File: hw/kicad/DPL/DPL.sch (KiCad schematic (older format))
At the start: 30 parts, among them J0 Programer, J1 DPL1, J2 DPL2, J3 DPL3, J4 DPL4, J5 DPL5, J6 DPL6, Q1 IRF540N, Q2 IRF540N, Q3 IRF540N, Q4 IRF540N, Q5 IRF540N, Q6 IRF540N, SW1 SW_Reed, SW2 SW_Reed, SW3 SW_Reed, SW4 SW_Reed, SW5 SW_Reed, SW6 SW_Reed, U0 SAMD21E, U1 Payload, Y1 32.768kHz

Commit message: Added power selector to the board. Started to design the footprint's layout.
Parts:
- added JP1: Power selector, Connector_PinHeader_2.54mm:PinHeader_1x03_P2.54mm_Vertical, symbol Device:Jumper_NC_Dual
- added R0: 1k, Resistor_THT:R_Axial_DIN0207_L6.3mm_D2.5mm_P10.16mm_Horizontal, symbol Device:R
- C1a1, C1b1: footprint (none) -> Capacitor_SMD:C_0603_1608Metric_Pad1.05x0.95mm_HandSolder
- J0: footprint (none) -> Connector_PinHeader_2.54mm:PinHeader_1x05_P2.54mm_Vertical
- J1, J2, J3, J4, J5, J6: footprint (none) -> TerminalBlock:TerminalBlock_Altech_AK300-2_P5.00mm
- R1, R2, R3, R4, R5, R6: footprint (none) -> Resistor_THT:R_Axial_DIN0207_L6.3mm_D2.5mm_P10.16mm_Horizontal
- SW1, SW2, SW3, SW4, SW5, SW6: footprint (none) -> Resistor_THT:R_Axial_DIN0309_L9.0mm_D3.2mm_P15.24mm_Horizontal
- U0: footprint (none) -> Package_QFP:TQFP-32_7x7mm_P0.8mm
- U1: footprint (none) -> Payload:PC104-Standard
- Y1: footprint (none) -> Crystal:Crystal_SMD_EuroQuartz_EQ161-2Pin_3.2x1.5mm_HandSoldering
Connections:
- net 3V3: now also R0.1
- net 5V0: now also JP1.3
- net SWCLK: now also R0.2
- net VBUS: now also JP1.1
- net VIN: now also JP1.2
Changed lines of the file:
@@
 F 0 "U1" H 9000 4798 50  0000 C CNN
 F 1 "Payload" H 9000 4707 50  0000 C CNN
-F 2 "" H 7900 4050 50  0001 C CNN
+F 2 "Payload:PC104-Standard" H 7900 4050 50  0001 C CNN
 F 3 "" H 7900 4050 50  0001 C CNN
 	1    9000 3250
@@
 F 0 "J1" H 1480 4442 50  0000 L CNN
 F 1 "DPL1" H 1480 4351 50  0000 L CNN
-F 2 "" H 1400 4450 50  0001 C CNN
+F 2 "TerminalBlock:TerminalBlock_Altech_AK300-2_P5.00mm" H 1400 4450 50  0001 C CNN
 F 3 "~" H 1400 4450 50  0001 C CNN
 	1    1400 4450
@@
 F 0 "J2" H 2630 4442 50  0000 L CNN
 F 1 "DPL2" H 2630 4351 50  0000 L CNN
-F 2 "" H 2550 4450 50  0001 C CNN
+F 2 "TerminalBlock:TerminalBlock_Altech_AK300-2_P5.00mm" H 2550 4450 50  0001 C CNN
 F 3 "~" H 2550 4450 50  0001 C CNN
 	1    2550 4450
@@
 F 0 "J3" H 3780 4442 50  0000 L CNN
 F 1 "DPL3" H 3780 4351 50  0000 L CNN
-F 2 "" H 3700 4450 50  0001 C CNN
+F 2 "TerminalBlock:TerminalBlock_Altech_AK300-2_P5.00mm" H 3700 4450 50  0001 C CNN
 F 3 "~" H 3700 4450 50  0001 C CNN
 	1    3700 4450
@@
 F 0 "J4" H 1480 5342 50  0000 L CNN
 F 1 "DPL4" H 1480 5251 50  0000 L CNN
-F 2 "" H 1400 5350 50  0001 C CNN
+F 2 "TerminalBlock:TerminalBlock_Altech_AK300-2_P5.00mm" H 1400 5350 50  0001 C CNN
 F 3 "~" H 1400 5350 50  0001 C CNN
 	1    1400 5350
@@
 F 0 "J5" H 2630 5342 50  0000 L CNN
 F 1 "DPL5" H 2630 5251 50  0000 L CNN
-F 2 "" H 2550 5350 50  0001 C CNN
+F 2 "TerminalBlock:TerminalBlock_Altech_AK300-2_P5.00mm" H 2550 5350 50  0001 C CNN
 F 3 "~" H 2550 5350 50  0001 C CNN
 	1    2550 5350
@@
 F 0 "J6" H 3780 5342 50  0000 L CNN
 F 1 "DPL6" H 3780 5251 50  0000 L CNN
-F 2 "" H 3700 5350 50  0001 C CNN
+F 2 "TerminalBlock:TerminalBlock_Altech_AK300-2_P5.00mm" H 3700 5350 50  0001 C CNN
 F 3 "~" H 3700 5350 50  0001 C CNN
 	1    3700 5350
@@
 F 0 "U0" H 5250 4215 50  0000 C CNN
 F 1 "SAMD21E" H 5250 4124 50  0000 C CNN
-F 2 "" H 5250 3100 50  0001 C CNN
+F 2 "Package_QFP:TQFP-32_7x7mm_P0.8mm" H 5250 3100 50  0001 C CNN
 F 3 "" H 5250 3100 50  0001 C CNN
 	1    5250 3200
@@
 F 0 "J0" H 4058 1681 50  0000 C CNN
 F 1 "Programer" H 4058 1590 50  0000 C CNN
-F 2 "" H 3950 1300 50  0001 C CNN
+F 2 "Connector_PinHeader_2.54mm:PinHeader_1x05_P2.54mm_Vertical" H 3950 1300 50  0001 C CNN
 F 3 "~" H 3950 1300 50  0001 C CNN
 	1    3950 1300
@@
 F 0 "Y1" H 3950 2768 50  0000 C CNN
 F 1 "32.768kHz" H 3950 2677 50  0000 C CNN
-F 2 "" H 3950 2500 50  0001 C CNN
+F 2 "Crystal:Crystal_SMD_EuroQuartz_EQ161-2Pin_3.2x1.5mm_HandSoldering" H 3950 2500 50  0001 C CNN
 F 3 "~" H 3950 2500 50  0001 C CNN
 	1    3950 2500
@@
 F 0 "C1b1" H 3715 2796 50  0000 L CNN
 F 1 "9pF" H 3715 2705 50  0000 L CNN
-F 2 "" H 3638 2600 50  0001 C CNN
+F 2 "Capacitor_SMD:C_0603_1608Metric_Pad1.05x0.95mm_HandSolder" H 3638 2600 50  0001 C CNN
 F 3 "~" H 3600 2750 50  0001 C CNN
 	1    3600 2750
@@
 F 0 "C1a1" H 3715 2296 50  0000 L CNN
 F 1 "9pF" H 3715 2205 50  0000 L CNN
-F 2 "" H 3638 2100 50  0001 C CNN
+F 2 "Capacitor_SMD:C_0603_1608Metric_Pad1.05x0.95mm_HandSolder" H 3638 2100 50  0001 C CNN
 F 3 "~" H 3600 2250 50  0001 C CNN
 	1    3600 2250
@@
 	1050 5000 1050 5050
 $Comp
-L power:GND #PWR?
+L power:GND #PWR0101
 U 1 1 5CF99838
 P 1050 5050
-F 0 "#PWR?" H 1050 4800 50  0001 C CNN
+F 0 "#PWR0101" H 1050 4800 50  0001 C CNN
 F 1 "GND" H 1055 4877 50  0000 C CNN
 F 2 "" H 1050 5050 50  0001 C CNN
@@
 	2200 5000 2200 5050
 $Comp
-L power:GND #PWR?
+L power:GND #PWR0104
 U 1 1 5CF9AF8D
 P 2200 5050
-F 0 "#PWR?" H 2200 4800 50  0001 C CNN
+F 0 "#PWR0104" H 2200 4800 50  0001 C CNN
 F 1 "GND" H 2205 4877 50  0000 C CNN
 F 2 "" H 2200 5050 50  0001 C CNN
@@
 	3350 5000 3350 5050
 $Comp
-L power:GND #PWR?
+L power:GND #PWR0105
 U 1 1 5CF9BBE1
 P 3350 5050
-F 0 "#PWR?" H 3350 4800 50  0001 C CNN
+F 0 "#PWR0105" H 3350 4800 50  0001 C CNN
 F 1 "GND" H 3355 4877 50  0000 C CNN
 F 2 "" H 3350 5050 50  0001 C CNN
@@
 	1050 5900 1050 5950
 $Comp
-L power:GND #PWR?
+L power:GND #PWR0106
 U 1 1 5CF9C528
 P 1050 5950
-F 0 "#PWR?" H 1050 5700 50  0001 C CNN
+F 0 "#PWR0106" H 1050 5700 50  0001 C CNN
 F 1 "GND" H 1055 5777 50  0000 C CNN
 F 2 "" H 1050 5950 50  0001 C CNN
@@
 	2350 5350 2200 5350
 $Comp
-L power:GND #PWR?
+L power:GND #PWR0109
 U 1 1 5CF9CBDF
 P 2200 5950
-F 0 "#PWR?" H 2200 5700 50  0001 C CNN
+F 0 "#PWR0109" H 2200 5700 50  0001 C CNN
 F 1 "GND" H 2205 5777 50  0000 C CNN
 F 2 "" H 2200 5950 50  0001 C CNN
@@
 	3350 5350 3500 5350
 $Comp
-L power:GND #PWR?
+L power:GND #PWR0110
 U 1 1 5CF9D59C
 P 3350 5950
-F 0 "#PWR?" H 3350 5700 50  0001 C CNN
+F 0 "#PWR0110" H 3350 5700 50  0001 C CNN
 F 1 "GND" H 3355 5777 50  0000 C CNN
 F 2 "" H 3350 5950 50  0001 C CNN
@@
 Connection ~ 3400 2750
 $Comp
-L power:GND #PWR?
+L power:GND #PWR0111
 U 1 1 5CF9C5E9
 P 3400 2800
-F 0 "#PWR?" H 3400 2550 50  0001 C CNN
+F 0 "#PWR0111" H 3400 2550 50  0001 C CNN
 F 1 "GND" H 3405 2627 50  0000 C CNN
 F 2 "" H 3400 2800 50  0001 C CNN
@@
 F 0 "SW1" H 4850 5672 50  0000 C CNN
 F 1 "SW_Reed" H 4850 5581 50  0000 C CNN
-F 2 "" H 4850 5450 50  0001 C CNN
+F 2 "Resistor_THT:R_Axial_DIN0309_L9.0mm_D3.2mm_P15.24mm_Horizontal" H 4850 5450 50  0001 C CNN
 F 3 "~" H 4850 5450 50  0001 C CNN
 	1    4850 5450
@@
 F 0 "SW2" H 4850 6022 50  0000 C CNN
 F 1 "SW_Reed" H 4850 5931 50  0000 C CNN
-F 2 "" H 4850 5800 50  0001 C CNN
+F 2 "Resistor_THT:R_Axial_DIN0309_L9.0mm_D3.2mm_P15.24mm_Horizontal" H 4850 5800 50  0001 C CNN
 F 3 "~" H 4850 5800 50  0001 C CNN
 	1    4850 5800
@@
 F 0 "SW3" H 4850 6372 50  0000 C CNN
 F 1 "SW_Reed" H 4850 6281 50  0000 C CNN
-F 2 "" H 4850 6150 50  0001 C CNN
+F 2 "Resistor_THT:R_Axial_DIN0309_L9.0mm_D3.2mm_P15.24mm_Horizontal" H 4850 6150 50  0001 C CNN
 F 3 "~" H 4850 6150 50  0001 C CNN
 	1    4850 6150
@@
 F 0 "SW4" H 4850 6722 50  0000 C CNN
 F 1 "SW_Reed" H 4850 6631 50  0000 C CNN
-F 2 "" H 4850 6500 50  0001 C CNN
+F 2 "Resistor_THT:R_Axial_DIN0309_L9.0mm_D3.2mm_P15.24mm_Horizontal" H 4850 6500 50  0001 C CNN
 F 3 "~" H 4850 6500 50  0001 C CNN
 	1    4850 6500
@@
 F 0 "SW5" H 4850 7072 50  0000 C CNN
 F 1 "SW_Reed" H 4850 6981 50  0000 C CNN
-F 2 "" H 4850 6850 50  0001 C CNN
+F 2 "Resistor_THT:R_Axial_DIN0309_L9.0mm_D3.2mm_P15.24mm_Horizontal" H 4850 6850 50  0001 C CNN
 F 3 "~" H 4850 6850 50  0001 C CNN
 	1    4850 6850
@@
 F 0 "SW6" H 4850 7422 50  0000 C CNN
 F 1 "SW_Reed" H 4850 7331 50  0000 C CNN
-F 2 "" H 4850 7200 50  0001 C CNN
+F 2 "Resistor_THT:R_Axial_DIN0309_L9.0mm_D3.2mm_P15.24mm_Horizontal" H 4850 7200 50  0001 C CNN
 F 3 "~" H 4850 7200 50  0001 C CNN
 	1    4850 7200
@@
 U 1 1 5CFAC755
 P 5800 5800
-F 0 "R2" H 5870 5846 50  0000 L CNN
-F 1 "1k" H 5870 5755 50  0000 L CNN
-F 2 "" V 5730 5800 50  0001 C CNN
+F 0 "R2" V 5900 5750 50  0000 L CNN
+F 1 "1k" V 5800 5750 50  0000 L CNN
+F 2 "Resistor_THT:R_Axial_DIN0207_L6.3mm_D2.5mm_P10.16mm_Horizontal" V 5730 5800 50  0001 C CNN
 F 3 "~" H 5800 5800 50  0001 C CNN
 	1    5800 5800
@@
 U 1 1 5CFAC7EA
 P 5800 6150
-F 0 "R3" H 5870 6196 50  0000 L CNN
-F 1 "1k" H 5870 6105 50  0000 L CNN
-F 2 "" V 5730 6150 50  0001 C CNN
+F 0 "R3" V 5900 6100 50  0000 L CNN
+F 1 "1k" V 5800 6100 50  0000 L CNN
+F 2 "Resistor_THT:R_Axial_DIN0207_L6.3mm_D2.5mm_P10.16mm_Horizontal" V 5730 6150 50  0001 C CNN
 F 3 "~" H 5800 6150 50  0001 C CNN
 	1    5800 6150
@@
 U 1 1 5CFAC8CF
 P 5800 6500
-F 0 "R4" H 5870 6546 50  0000 L CNN
-F 1 "1k" H 5870 6455 50  0000 L CNN
-F 2 "" V 5730 6500 50  0001 C CNN
+F 0 "R4" V 5900 6450 50  0000 L CNN
+F 1 "1k" V 5800 6450 50  0000 L CNN
+F 2 "Resistor_THT:R_Axial_DIN0207_L6.3mm_D2.5mm_P10.16mm_Horizontal" V 5730 6500 50  0001 C CNN
 F 3 "~" H 5800 6500 50  0001 C CNN
 	1    5800 6500
@@
 U 1 1 5CFACA54
 P 5800 6850
-F 0 "R5" H 5870 6896 50  0000 L CNN
-F 1 "1k" H 5870 6805 50  0000 L CNN
-F 2 "" V 5730 6850 50  0001 C CNN
+F 0 "R5" V 5900 6800 50  0000 L CNN
+F 1 "1k" V 5800 6800 50  0000 L CNN
+F 2 "Resistor_THT:R_Axial_DIN0207_L6.3mm_D2.5mm_P10.16mm_Horizontal" V 5730 6850 50  0001 C CNN
 F 3 "~" H 5800 6850 50  0001 C CNN
 	1    5800 6850
@@
 U 1 1 5CFAD116
 P 5800 7200
-F 0 "R6" H 5870 7246 50  0000 L CNN
-F 1 "1k" H 5870 7155 50  0000 L CNN
-F 2 "" V 5730 7200 50  0001 C CNN
+F 0 "R6" V 5900 7150 50  0000 L CNN
+F 1 "1k" V 5800 7150 50  0000 L CNN
+F 2 "Resistor_THT:R_Axial_DIN0207_L6.3mm_D2.5mm_P10.16mm_Horizontal" V 5730 7200 50  0001 C CNN
 F 3 "~" H 5800 7200 50  0001 C CNN
 	1    5800 7200
@@
 Connection ~ 6000 7200
 $Comp
-L power:GND #PWR?
+L power:GND #PWR0112
 U 1 1 5CFB9A35
 P 6000 7250
-F 0 "#PWR?" H 6000 7000 50  0001 C CNN
+F 0 "#PWR0112" H 6000 7000 50  0001 C CNN
 F 1 "GND" H 6005 7077 50  0000 C CNN
 F 2 "" H 6000 7250 50  0001 C CNN
@@
 U 1 1 5CFB9EE2
 P 5800 5450
-F 0 "R1" H 5870 5496 50  0000 L CNN
-F 1 "1k" H 5870 5405 50  0000 L CNN
-F 2 "" V 5730 5450 50  0001 C CNN
+F 0 "R1" V 5900 5400 50  0000 L CNN
+F 1 "1k" V 5800 5400 50  0000 L CNN
+F 2 "Resistor_THT:R_Axial_DIN0207_L6.3mm_D2.5mm_P10.16mm_Horizontal" V 5730 5450 50  0001 C CNN
 F 3 "~" H 5800 5450 50  0001 C CNN
 	1    5800 5450
@@
 Wire Wire Line
 	6050 3750 6600 3750
+$Comp
+L Device:R R0
+U 1 1 5CFACF42
+P 4600 1200
+F 0 "R0" V 4500 1200 50  0000 C CNN
+F 1 "1k" V 4600 1200 50  0000 C CNN
+F 2 "Resistor_THT:R_Axial_DIN0207_L6.3mm_D2.5mm_P10.16mm_Horizontal" V 4530 1200 50  0001 C CNN
+F 3 "~" H 4600 1200 50  0001 C CNN
+	1    4600 1200
+	0    1    1    0
+$EndComp
+Text Label 4950 1200 2    50   ~ 0
+3V3
+Wire Wire Line
+	4950 1200 4750 1200
+$Comp
+L Device:Jumper_NC_Dual JP1
+U 1 1 5CFEFE3B
+P 2600 1300
+F 0 "JP1" H 2600 1539 50  0000 C CNN
+F 1 "Power selector" H 2600 1448 50  0000 C CNN
+F 2 "Connector_PinHeader_2.54mm:PinHeader_1x03_P2.54mm_Vertical" H 2600 1300 50  0001 C CNN
+F 3 "~" H 2600 1300 50  0001 C CNN
+	1    2600 1300
+	1    0    0    -1
+$EndComp
+Text Label 2100 1300 0    50   ~ 0
+VBUS
+Text Label 3050 1300 2    50   ~ 0
+5V0
+Text Label 2800 1450 2    50   ~ 0
+VIN
+Wire Wire Line
+	2100 1300 2350 1300
+Wire Wire Line
+	2600 1400 2600 1450
+Wire Wire Line
+	2600 1450 2800 1450
+Wire Wire Line
+	2850 1300 3050 1300
 $EndSCHEMATC

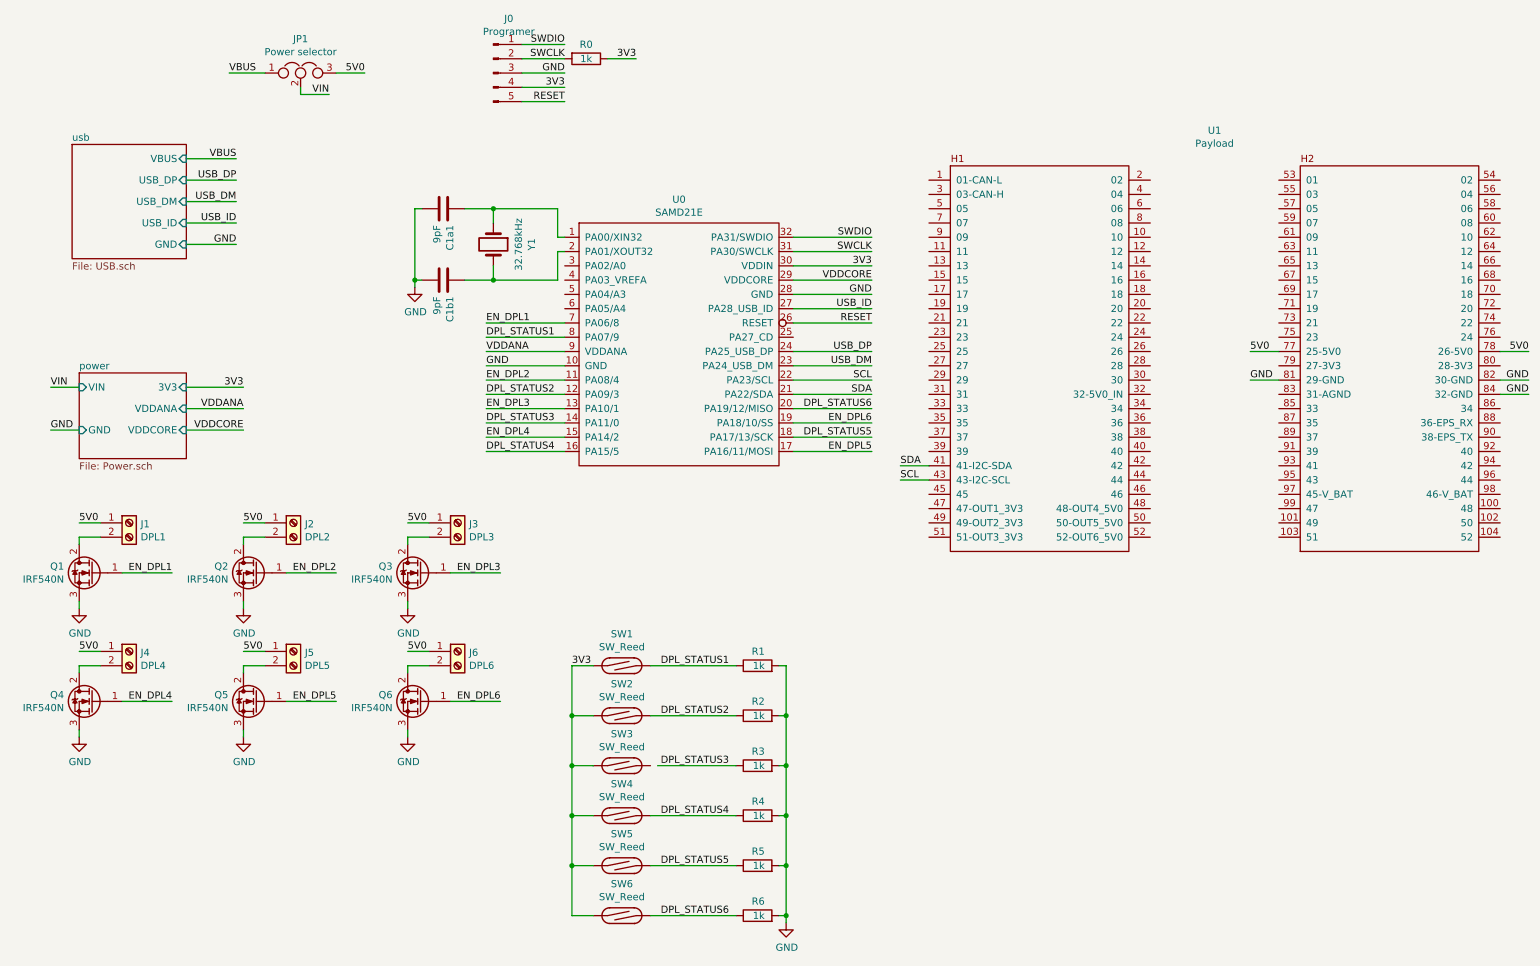
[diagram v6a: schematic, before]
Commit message: Fixed some conections errors. Designed the footprint. Added vias to pass the thread wire of the balloons through them.
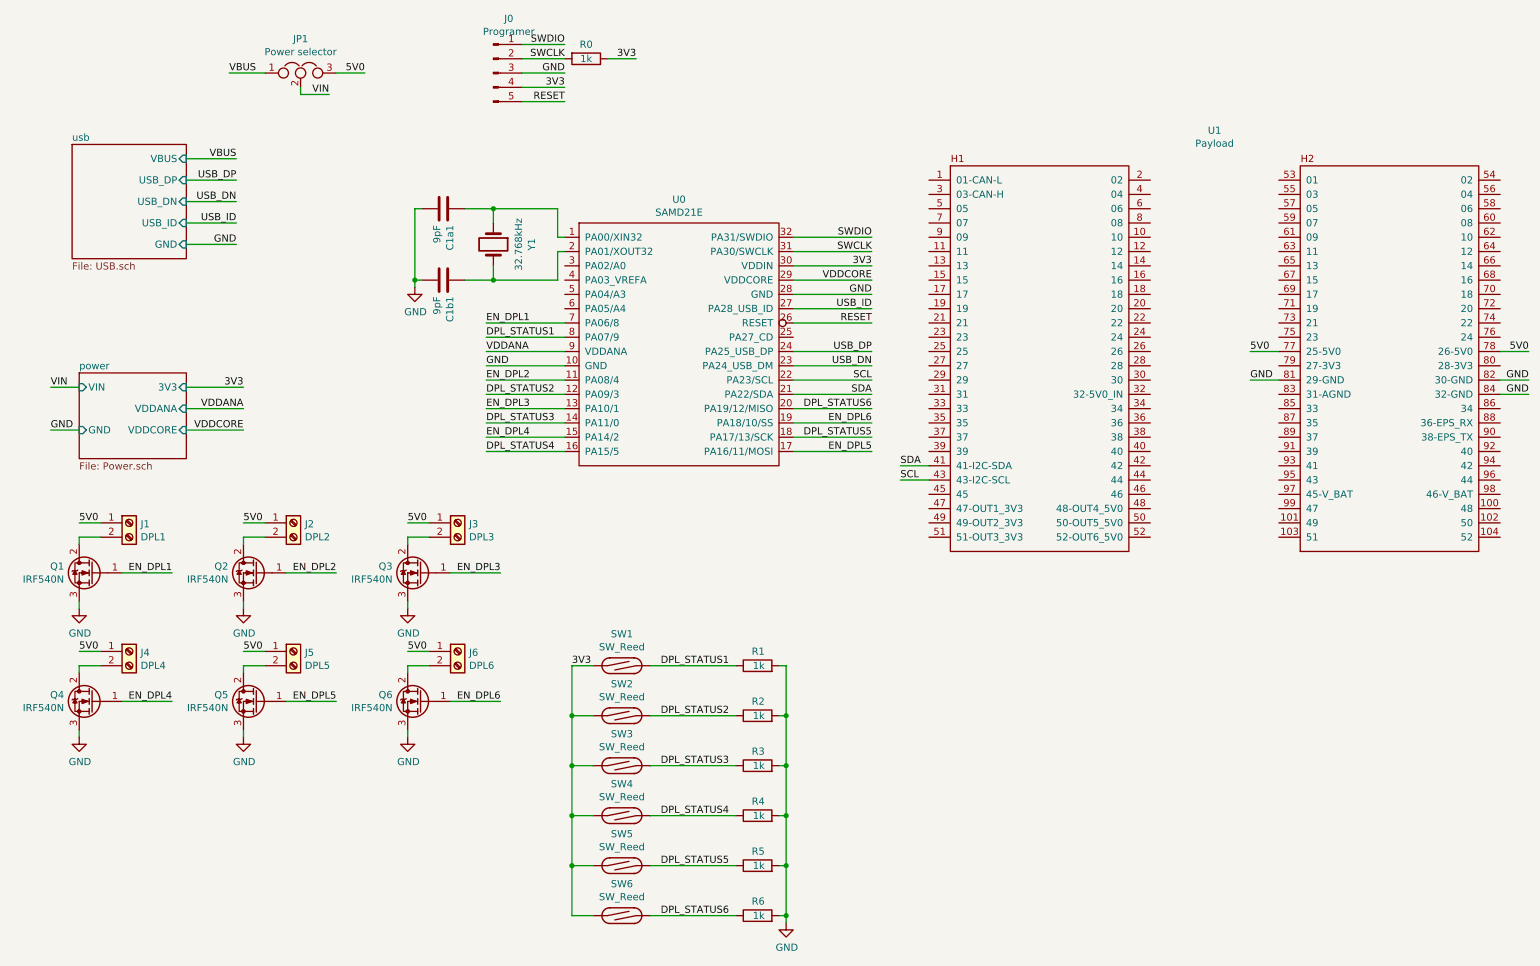
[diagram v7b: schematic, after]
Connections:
- net DPL_STATUS3: now also SW3.2
- net USB_DM renamed USB_DN
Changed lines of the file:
@@
 F2 "VBUS" I R 1800 1900 50
 F3 "USB_DP" I R 1800 2050 50
-F4 "USB_DM" I R 1800 2200 50
+F4 "USB_DN" I R 1800 2200 50
 F5 "USB_ID" I R 1800 2350 50
 F6 "GND" I R 1800 2500 50
@@
 USB_DP
 Text Label 2150 2200 2    50   ~ 0
-USB_DM
+USB_DN
 Text Label 2150 2350 2    50   ~ 0
 USB_ID
@@
 USB_DP
 Text Label 6600 3350 2    50   ~ 0
-USB_DM
+USB_DN
 Text Label 6600 2950 2    50   ~ 0
 USB_ID
@@
 Wire Wire Line
 	5650 5800 5050 5800
-Wire Wire Line
-	5100 6150 5650 6150
 Wire Wire Line
 	5650 6500 5050 6500
@@
 Wire Wire Line
 	2850 1300 3050 1300
+Wire Wire Line
+	5050 6150 5650 6150
 $EndSCHEMATC

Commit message: Adding level shifter.
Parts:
- added J8: BATT, TerminalBlock:TerminalBlock_Altech_AK300-2_P5.00mm, symbol Connector:Screw_Terminal_01x02
- added J9: Level shifter, symbol Connector_Generic:Conn_02x06_Counter_Clockwise
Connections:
- net labels added: LV1, LV2, LV3, LV4, VBATT
- wire segments 125 -> 140
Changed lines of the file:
@@
 	1050 4550 1200 4550
 Text Label 1050 4450 0    50   ~ 0
-5V0
+VBATT
 Wire Wire Line
 	2200 4600 2200 4550
@@
 	2200 4550 2350 4550
 Text Label 2200 4450 0    50   ~ 0
-5V0
+VBATT
 Wire Wire Line
 	3350 4600 3350 4550
@@
 	3350 4550 3500 4550
 Text Label 3350 4450 0    50   ~ 0
-5V0
+VBATT
 Wire Wire Line
 	1050 5450 1200 5450
@@
 	1050 5450 1050 5500
 Text Label 1050 5350 0    50   ~ 0
-5V0
+VBATT
 Wire Wire Line
 	2200 5500 2200 5450
@@
 	2200 5450 2350 5450
 Text Label 2200 5350 0    50   ~ 0
-5V0
+VBATT
 Wire Wire Line
 	3350 5500 3350 5450
@@
 	3350 5450 3500 5450
 Text Label 3350 5350 0    50   ~ 0
-5V0
+VBATT
 Wire Wire Line
 	1200 4450 1050 4450
@@
 Wire Wire Line
 	5050 6150 5650 6150
+$Comp
+L Connector:Screw_Terminal_01x02 J8
+U 1 1 5D028190
+P 2550 4000
+F 0 "J8" H 2630 3992 50  0000 L CNN
+F 1 "BATT" H 2630 3901 50  0000 L CNN
+F 2 "TerminalBlock:TerminalBlock_Altech_AK300-2_P5.00mm" H 2550 4000 50  0001 C CNN
+F 3 "~" H 2550 4000 50  0001 C CNN
+	1    2550 4000
+	-1   0    0    -1
+$EndComp
+Text Label 3000 4000 2    50   ~ 0
+VBATT
+Wire Wire Line
+	2750 4000 3000 4000
+$Comp
+L power:GND #PWR?
+U 1 1 5D02A6CC
+P 2800 4150
+F 0 "#PWR?" H 2800 3900 50  0001 C CNN
+F 1 "GND" H 2805 3977 50  0000 C CNN
+F 2 "" H 2800 4150 50  0001 C CNN
+F 3 "" H 2800 4150 50  0001 C CNN
+	1    2800 4150
+	1    0    0    -1
+$EndComp
+Wire Wire Line
+	2800 4150 2800 4100
+Wire Wire Line
+	2800 4100 2750 4100
+$Comp
+L Connector_Generic:Conn_02x06_Counter_Clockwise J9
+U 1 1 5D019702
+P 2200 6800
+F 0 "J9" H 2250 7217 50  0000 C CNN
+F 1 "Level shifter" H 2250 7126 50  0000 C CNN
+F 2 "" H 2200 6800 50  0001 C CNN
+F 3 "~" H 2200 6800 50  0001 C CNN
+	1    2200 6800
+	1    0    0    -1
+$EndComp
+Text Label 1650 6800 0    50   ~ 0
+GND
+Text Label 2700 6800 2    50   ~ 0
+GND
+Text Label 2700 6900 2    50   ~ 0
+3V3
+Text Label 1650 6900 0    50   ~ 0
+VIN
+Text Label 2700 7100 2    50   ~ 0
+LV1
+Text Label 2700 7000 2    50   ~ 0
+LV2
+Text Label 2700 6700 2    50   ~ 0
+LV3
+Text Label 2700 6600 2    50   ~ 0
+LV4
+Text Label 1650 7100 0    50   ~ 0
+EN_DPL1
+Text Label 1650 7000 0    50   ~ 0
+EN_DPL2
+Text Label 1650 6700 0    50   ~ 0
+EN_DPL3
+Text Label 1650 6600 0    50   ~ 0
+EN_DPL4
+Wire Wire Line
+	2700 7100 2500 7100
+Wire Wire Line
+	2500 7000 2700 7000
+Wire Wire Line
+	2700 6900 2500 6900
+Wire Wire Line
+	2500 6800 2700 6800
+Wire Wire Line
+	2700 6700 2500 6700
+Wire Wire Line
+	2500 6600 2700 6600
+Wire Wire Line
+	1650 6700 2000 6700
+Wire Wire Line
+	2000 6800 1650 6800
+Wire Wire Line
+	1650 6900 2000 6900
+Wire Wire Line
+	2000 7000 1650 7000
+Wire Wire Line
+	1650 6600 2000 6600
+Wire Wire Line
+	1650 7100 2000 7100
 $EndSCHEMATC
